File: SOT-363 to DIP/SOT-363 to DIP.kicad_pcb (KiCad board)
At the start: 2 copper layers, 13.8 x 10.2 mm, 4 parts, among them J1 SOT-363, J2 Conn_01x03_Pin, J3 Conn_01x03_Pin, J4 SOT-353

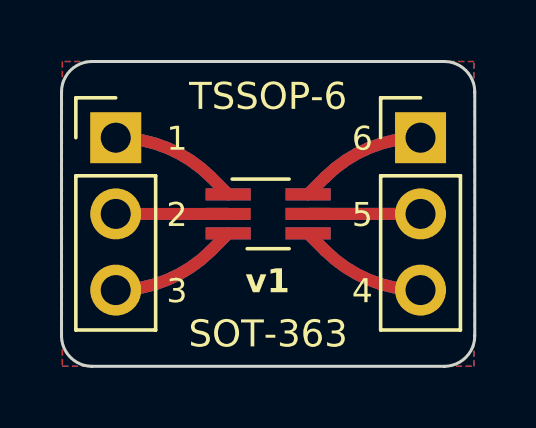
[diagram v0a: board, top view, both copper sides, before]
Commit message: Remove silkscreen of pin headers
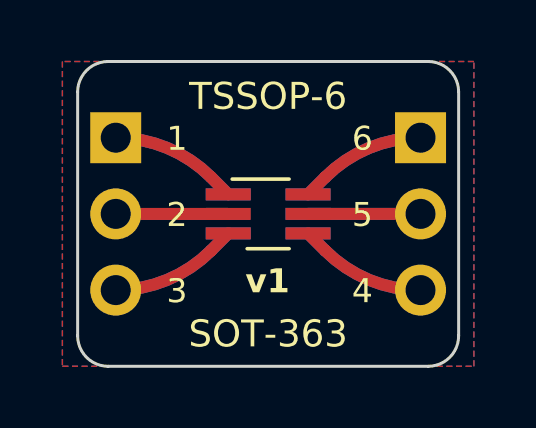
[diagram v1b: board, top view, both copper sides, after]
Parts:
- J2, J3: footprint Connector_PinHeader_2.54mm:PinHeader_1x03_P2.54mm_Vertical -> _footprints:PinHeader_1x03_P2.54mm_Vertical_nosilk
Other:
- board size 13.8 x 10.2 mm -> 12.7 x 10.2 mm
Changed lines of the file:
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@@
   (net 5 "/Pin 5")
   (net 6 "/Pin 6")
-  (footprint "Connector_PinHeader_2.54mm:PinHeader_1x03_P2.54mm_Vertical" (layer "F.Cu")
+  (footprint "_footprints:PinHeader_1x03_P2.54mm_Vertical_nosilk" (layer "F.Cu")
     (at 116.84 88.9)
     (descr "Through hole straight pin header, 1x03, 2.54mm pitch, single row")
@@
         (effects (font (size 1 1) (thickness 0.15)))
     )
-    (fp_line (start -1.33 -1.33) (end 0 -1.33)
-      (stroke (width 0.12) (type solid)) (layer "F.SilkS"))
-    (fp_line (start -1.33 0) (end -1.33 -1.33)
-      (stroke (width 0.12) (type solid)) (layer "F.SilkS"))
-    (fp_line (start -1.33 1.27) (end -1.33 6.41)
-      (stroke (width 0.12) (type solid)) (layer "F.SilkS"))
-    (fp_line (start -1.33 1.27) (end 1.33 1.27)
-      (stroke (width 0.12) (type solid)) (layer "F.SilkS"))
-    (fp_line (start -1.33 6.41) (end 1.33 6.41)
-      (stroke (width 0.12) (type solid)) (layer "F.SilkS"))
-    (fp_line (start 1.33 1.27) (end 1.33 6.41)
-      (stroke (width 0.12) (type solid)) (layer "F.SilkS"))
     (fp_line (start -1.8 -1.8) (end -1.8 6.85)
       (stroke (width 0.05) (type solid)) (layer "F.CrtYd"))
@@
     )
   )
-  (footprint "Connector_PinHeader_2.54mm:PinHeader_1x03_P2.54mm_Vertical" (layer "F.Cu")
+  (footprint "_footprints:PinHeader_1x03_P2.54mm_Vertical_nosilk" (layer "F.Cu")
     (at 127 88.9)
     (descr "Through hole straight pin header, 1x03, 2.54mm pitch, single row")
@@
         (effects (font (size 1 1) (thickness 0.15)))
     )
-    (fp_line (start -1.33 -1.33) (end 0 -1.33)
-      (stroke (width 0.12) (type solid)) (layer "F.SilkS"))
-    (fp_line (start -1.33 0) (end -1.33 -1.33)
-      (stroke (width 0.12) (type solid)) (layer "F.SilkS"))
-    (fp_line (start -1.33 1.27) (end -1.33 6.41)
-      (stroke (width 0.12) (type solid)) (layer "F.SilkS"))
-    (fp_line (start -1.33 1.27) (end 1.33 1.27)
-      (stroke (width 0.12) (type solid)) (layer "F.SilkS"))
-    (fp_line (start -1.33 6.41) (end 1.33 6.41)
-      (stroke (width 0.12) (type solid)) (layer "F.SilkS"))
-    (fp_line (start 1.33 1.27) (end 1.33 6.41)
-      (stroke (width 0.12) (type solid)) (layer "F.SilkS"))
     (fp_line (start -1.8 -1.8) (end -1.8 6.85)
       (stroke (width 0.05) (type solid)) (layer "F.CrtYd"))
@@
     )
   )
-  (gr_rect (start 115.5099 90.17) (end 118.1699 95.31)
-    (stroke (width 0.12) (type default)) (fill none) (layer "B.SilkS"))
-  (gr_line (start 118.1699 87.57) (end 118.1699 88.9)
-    (stroke (width 0.12) (type default)) (layer "B.SilkS"))
-  (gr_line (start 127 87.57) (end 128.33 87.57)
-    (stroke (width 0.12) (type default)) (layer "B.SilkS"))
-  (gr_line (start 116.8399 87.57) (end 118.1699 87.57)
-    (stroke (width 0.12) (type default)) (layer "B.SilkS"))
-  (gr_rect (start 125.67 90.17) (end 128.33 95.31)
-    (stroke (width 0.12) (type default)) (fill none) (layer "B.SilkS"))
-  (gr_line (start 128.33 87.57) (end 128.33 88.9)
-    (stroke (width 0.12) (type default)) (layer "B.SilkS"))
-  (gr_arc (start 127.792 86.36) (mid 128.51042 86.65758) (end 128.808 87.376)
-    (stroke (width 0.1) (type default)) (layer "Edge.Cuts"))
-  (gr_line (start 115.032 95.504) (end 115.032 87.376)
-    (stroke (width 0.1) (type default)) (layer "Edge.Cuts"))
-  (gr_arc (start 128.808 95.504) (mid 128.51042 96.22242) (end 127.792 96.52)
-    (stroke (width 0.1) (type default)) (layer "Edge.Cuts"))
-  (gr_arc (start 116.048 96.52) (mid 115.32958 96.22242) (end 115.032 95.504)
-    (stroke (width 0.1) (type default)) (layer "Edge.Cuts"))
-  (gr_arc (start 115.032 87.376) (mid 115.32958 86.65758) (end 116.048 86.36)
-    (stroke (width 0.1) (type default)) (layer "Edge.Cuts"))
-  (gr_line (start 128.808 87.376) (end 128.808 95.504)
-    (stroke (width 0.1) (type default)) (layer "Edge.Cuts"))
-  (gr_line (start 127.792 96.52) (end 116.048 96.52)
-    (stroke (width 0.1) (type default)) (layer "Edge.Cuts"))
-  (gr_line (start 116.048 86.36) (end 127.792 86.36)
+  (gr_arc (start 127.254 86.36) (mid 127.97242 86.65758) (end 128.27 87.376)
+    (stroke (width 0.1) (type default)) (layer "Edge.Cuts"))
+  (gr_line (start 115.57 95.504) (end 115.57 87.376)
+    (stroke (width 0.1) (type default)) (layer "Edge.Cuts"))
+  (gr_arc (start 128.27 95.504) (mid 127.97242 96.22242) (end 127.254 96.52)
+    (stroke (width 0.1) (type default)) (layer "Edge.Cuts"))
+  (gr_arc (start 116.586 96.52) (mid 115.86758 96.22242) (end 115.57 95.504)
+    (stroke (width 0.1) (type default)) (layer "Edge.Cuts"))
+  (gr_arc (start 115.57 87.376) (mid 115.86758 86.65758) (end 116.586 86.36)
+    (stroke (width 0.1) (type default)) (layer "Edge.Cuts"))
+  (gr_line (start 128.27 87.376) (end 128.27 95.504)
+    (stroke (width 0.1) (type default)) (layer "Edge.Cuts"))
+  (gr_line (start 127.254 96.52) (end 116.586 96.52)
+    (stroke (width 0.1) (type default)) (layer "Edge.Cuts"))
+  (gr_line (start 116.586 86.36) (end 127.254 86.36)
     (stroke (width 0.1) (type default)) (layer "Edge.Cuts"))
   (gr_text "2" (at 124.96 91.94) (layer "B.SilkS")
@@
     )
   )
-  (group "" (id 49c63f70-7b33-4d1a-a62a-e39d6e66d2fd)
-    (members
-      68b317da-d48f-46e8-ab9d-9ee216e7b2a5
-      6d7bbcb5-4782-4f8f-b6b1-d32889530b7d
-      c4ae07da-9613-4ccd-8237-50aa289d6cb7
-    )
-  )
-  (group "" (id edc9c157-df5d-4cb8-bd71-a43d2e88d545)
-    (members
-      b658a185-79d5-45e6-805b-a888af1587bf
-      d1b59d23-a1b3-4f95-ad51-96eb76bdc3fd
-      d7005366-bdc0-4a22-b393-b7730696f121
-    )
-  )

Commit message: Decrease height to 10mm
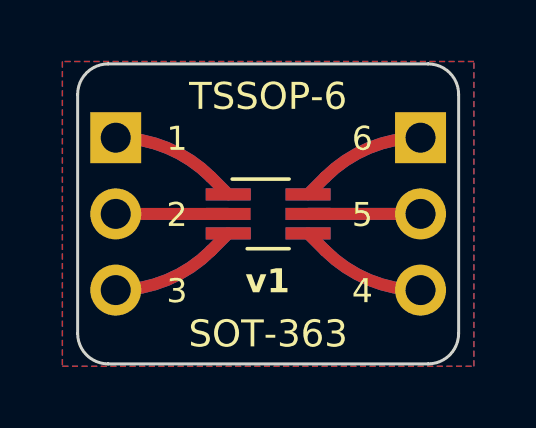
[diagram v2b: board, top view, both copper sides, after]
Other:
- board size 12.7 x 10.2 mm -> 12.7 x 10 mm
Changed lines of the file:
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@@
     )
   )
-  (gr_arc (start 127.254 86.36) (mid 127.97242 86.65758) (end 128.27 87.376)
+  (gr_arc (start 127.254 86.44) (mid 127.97242 86.73758) (end 128.27 87.456)
     (stroke (width 0.1) (type default)) (layer "Edge.Cuts"))
-  (gr_line (start 115.57 95.504) (end 115.57 87.376)
+  (gr_line (start 115.57 95.424) (end 115.57 87.456)
     (stroke (width 0.1) (type default)) (layer "Edge.Cuts"))
-  (gr_arc (start 128.27 95.504) (mid 127.97242 96.22242) (end 127.254 96.52)
+  (gr_arc (start 128.27 95.424) (mid 127.97242 96.14242) (end 127.254 96.44)
     (stroke (width 0.1) (type default)) (layer "Edge.Cuts"))
-  (gr_arc (start 116.586 96.52) (mid 115.86758 96.22242) (end 115.57 95.504)
+  (gr_arc (start 116.586 96.44) (mid 115.86758 96.14242) (end 115.57 95.424)
     (stroke (width 0.1) (type default)) (layer "Edge.Cuts"))
-  (gr_arc (start 115.57 87.376) (mid 115.86758 86.65758) (end 116.586 86.36)
+  (gr_arc (start 115.57 87.456) (mid 115.86758 86.73758) (end 116.586 86.44)
     (stroke (width 0.1) (type default)) (layer "Edge.Cuts"))
-  (gr_line (start 128.27 87.376) (end 128.27 95.504)
+  (gr_line (start 128.27 87.456) (end 128.27 95.424)
     (stroke (width 0.1) (type default)) (layer "Edge.Cuts"))
-  (gr_line (start 127.254 96.52) (end 116.586 96.52)
+  (gr_line (start 127.254 96.44) (end 116.586 96.44)
     (stroke (width 0.1) (type default)) (layer "Edge.Cuts"))
-  (gr_line (start 116.586 86.36) (end 127.254 86.36)
+  (gr_line (start 116.586 86.44) (end 127.254 86.44)
     (stroke (width 0.1) (type default)) (layer "Edge.Cuts"))
   (gr_text "2" (at 124.96 91.94) (layer "B.SilkS")
